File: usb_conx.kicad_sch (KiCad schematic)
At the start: 9 parts, among them J57 USB_B_Micro, J58 Conn_01x04, U30 TS3USB3000RSE, U31 AP22653AW6-7

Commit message: Replace micro-usb connectors with horizontal ones
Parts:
- J57: footprint HL_Connector_USB:MICRO-USB-SMD_MICRO-21-P2-T3 -> HL_Connector_USB:MICRO-USB-SMD_MICROXNJ; LCSC C2834965 -> C404969
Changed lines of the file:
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@@
 			)
 		)
-		(property "Footprint" "HL_Connector_USB:MICRO-USB-SMD_MICRO-21-P2-T3"
+		(property "Footprint" "HL_Connector_USB:MICRO-USB-SMD_MICROXNJ"
 			(at 114.3 76.2 0)
 			(effects
@@
 			)
 		)
-		(property "LCSC" "C2834965"
+		(property "LCSC" "C404969"
 			(at 110.49 74.93 0)
 			(effects

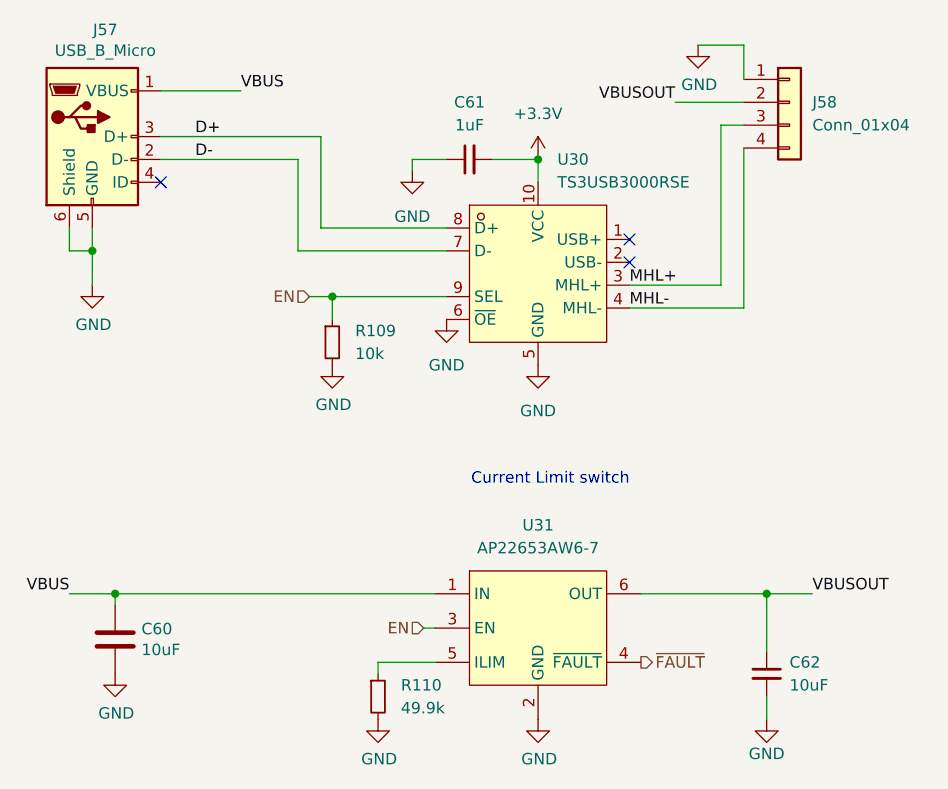
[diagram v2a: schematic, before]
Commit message: Update the design to a stackable one
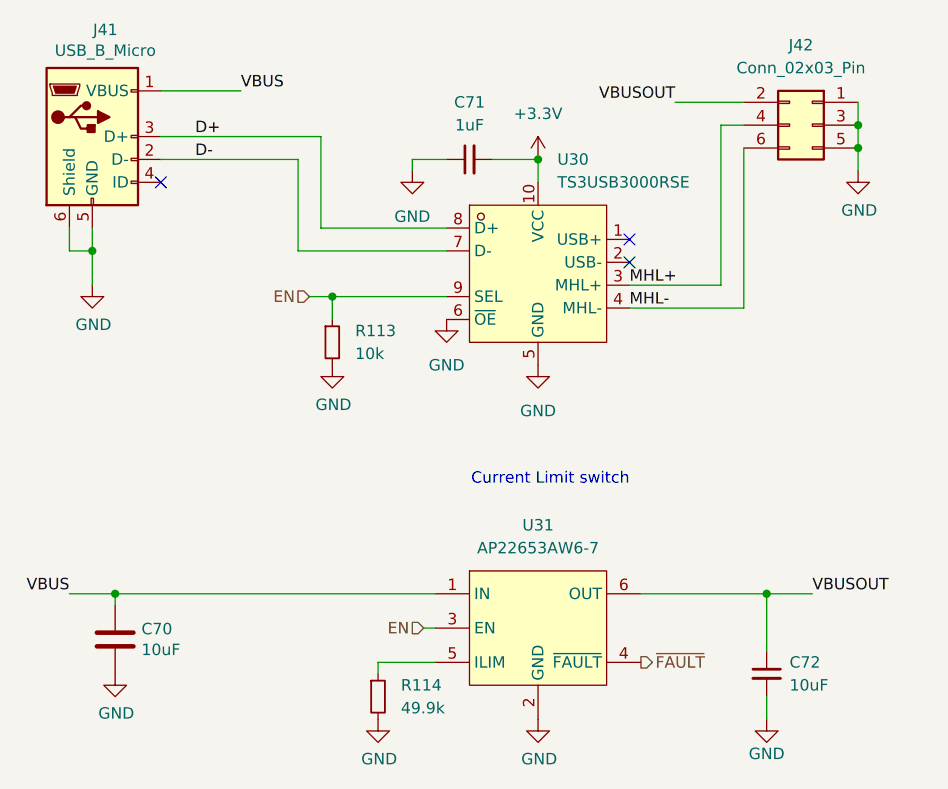
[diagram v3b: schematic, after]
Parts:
- J41: renamed from J57; footprint HL_Connector_USB:MICRO-USB-SMD_MICROXNJ -> HL_Connector_USB:MICRO-USB-SMD_920-154A2021Y10109; LCSC C404969 -> C399946
- J42: renamed from J58; value Conn_01x04 -> Conn_02x03_Pin; footprint HL_Connector_Pad_2.54mm:Pad_1x04_P2.54_1.7x1.7_Rect-Rnd-Oct-Oct -> HL_Connector_Pad_2.54mm:Pad_2x03_P2.54_1.7x1.7_Rect-1Rnd-2Oct_Mirror; symbol Connector_Generic:Conn_01x04 -> Connector_Generic:Conn_02x03_Odd_Even; JLCPCB_CORRECTION 0;3.81;270 -> 1.27;-2.54;270; LCSC C2691448 -> C2685197
- renumbered C60 to C70, C61 to C71, C62 to C72, R109 to R113, R110 to R114
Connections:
- net GND: now also J42.3 (Pin_3), J42.5 (Pin_5)
- net MHL+: now also J42.4 (Pin_4); no longer J42.3 (Pin_3)
- net MHL-: now also J42.6 (Pin_6); no longer J42.4 (Pin_4)
